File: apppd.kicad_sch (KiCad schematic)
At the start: 99 parts, among them J1 Conn_SWD, J2 APPPD Connector, J4 2601-1102, J5 USB_C_Receptacle_USB2.0_16P, Q1 AO3400A, Q2 AO3400A, Q3 PMV100EPA, SW1 NRST, SW2 BOOT0, U1 AP2112K-3.3, U2 STM32F072CBTx, U3 USBLC6-2SC6, U4 TCAN337, U5 TLV9062xD, U6 LMR33610ADDAR, U7 TLV9062xD, Y1 ABM8AIG-24.000MHz-8-2Z-T

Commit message: update
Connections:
- net GND: now also C29.1
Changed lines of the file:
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@@
 	(text "SMPS"
 		(exclude_from_sim no)
-		(at 244.602 143.002 0)
+		(at 242.824 142.24 0)
 		(effects
 			(font
@@
 	)
 	(symbol
+		(lib_id "Device:C")
+		(at 172.72 226.06 180)
+		(unit 1)
+		(body_style 1)
+		(exclude_from_sim no)
+		(in_bom yes)
+		(on_board yes)
+		(in_pos_files yes)
+		(dnp no)
+		(property "Reference" "C29"
+			(at 175.006 224.79 0)
+			(show_name no)
+			(do_not_autoplace no)
+			(effects
+				(font
+					(size 1.27 1.27)
+				)
+				(justify right)
+			)
+		)
+		(property "Value" "100nF"
+			(at 175.006 227.33 0)
+			(show_name no)
+			(do_not_autoplace no)
+			(effects
+				(font
+					(size 1.27 1.27)
+				)
+				(justify right)
+			)
+		)
+		(property "Footprint" "Capacitor_SMD:C_0402_1005Metric_Pad0.74x0.62mm_HandSolder"
+			(at 171.7548 222.25 0)
+			(hide yes)
+			(show_name no)
+			(do_not_autoplace no)
+			(effects
+				(font
+					(size 1.27 1.27)
+				)
+			)
+		)
+		(property "Datasheet" ""
+			(at 172.72 226.06 0)
+			(hide yes)
+			(show_name no)
+			(do_not_autoplace no)
+			(effects
+				(font
+					(size 1.27 1.27)
+				)
+			)
+		)
+		(property "Description" "Unpolarized capacitor"
+			(at 172.72 226.06 0)
+			(hide yes)
+			(show_name no)
+			(do_not_autoplace no)
+			(effects
+				(font
+					(size 1.27 1.27)
+				)
+			)
+		)
+		(pin "2"
+		)
+		(pin "1"
+		)
+		(instances
+			(project "apppd"
+				(path "/a8b9181f-aad2-4ac0-b955-77d7b04bcf42"
+					(reference "C29")
+					(unit 1)
+				)
+			)
+		)
+	)
+	(symbol
 		(lib_id "power:+12V")
 		(at 186.69 151.13 0)
@@
 					(unit 1)
 				)
-			)
-		)
-	)
-	(symbol
-		(lib_id "Device:C")
-		(at 172.72 224.79 180)
-		(unit 1)
-		(body_style 1)
-		(exclude_from_sim no)
-		(in_bom yes)
-		(on_board yes)
-		(in_pos_files yes)
-		(dnp no)
-		(property "Reference" "C29"
-			(at 175.006 223.52 0)
-			(show_name no)
-			(do_not_autoplace no)
-			(effects
-				(font
-					(size 1.27 1.27)
-				)
-				(justify right)
-			)
-		)
-		(property "Value" "100nF"
-			(at 175.006 226.06 0)
-			(show_name no)
-			(do_not_autoplace no)
-			(effects
-				(font
-					(size 1.27 1.27)
-				)
-				(justify right)
-			)
-		)
-		(property "Footprint" "Capacitor_SMD:C_0402_1005Metric_Pad0.74x0.62mm_HandSolder"
-			(at 171.7548 220.98 0)
-			(hide yes)
-			(show_name no)
-			(do_not_autoplace no)
-			(effects
-				(font
-					(size 1.27 1.27)
-				)
-			)
-		)
-		(property "Datasheet" ""
-			(at 172.72 224.79 0)
-			(hide yes)
-			(show_name no)
-			(do_not_autoplace no)
-			(effects
-				(font
-					(size 1.27 1.27)
-				)
-			)
-		)
-		(property "Description" "Unpolarized capacitor"
-			(at 172.72 224.79 0)
-			(hide yes)
-			(show_name no)
-			(do_not_autoplace no)
-			(effects
-				(font
-					(size 1.27 1.27)
-				)
-			)
-		)
-		(pin "2"
-		)
-		(pin "1"
-		)
-		(instances
-			(project "apppd"
-				(path "/a8b9181f-aad2-4ac0-b955-77d7b04bcf42"
-					(reference "C29")
-					(unit 1)
-				)

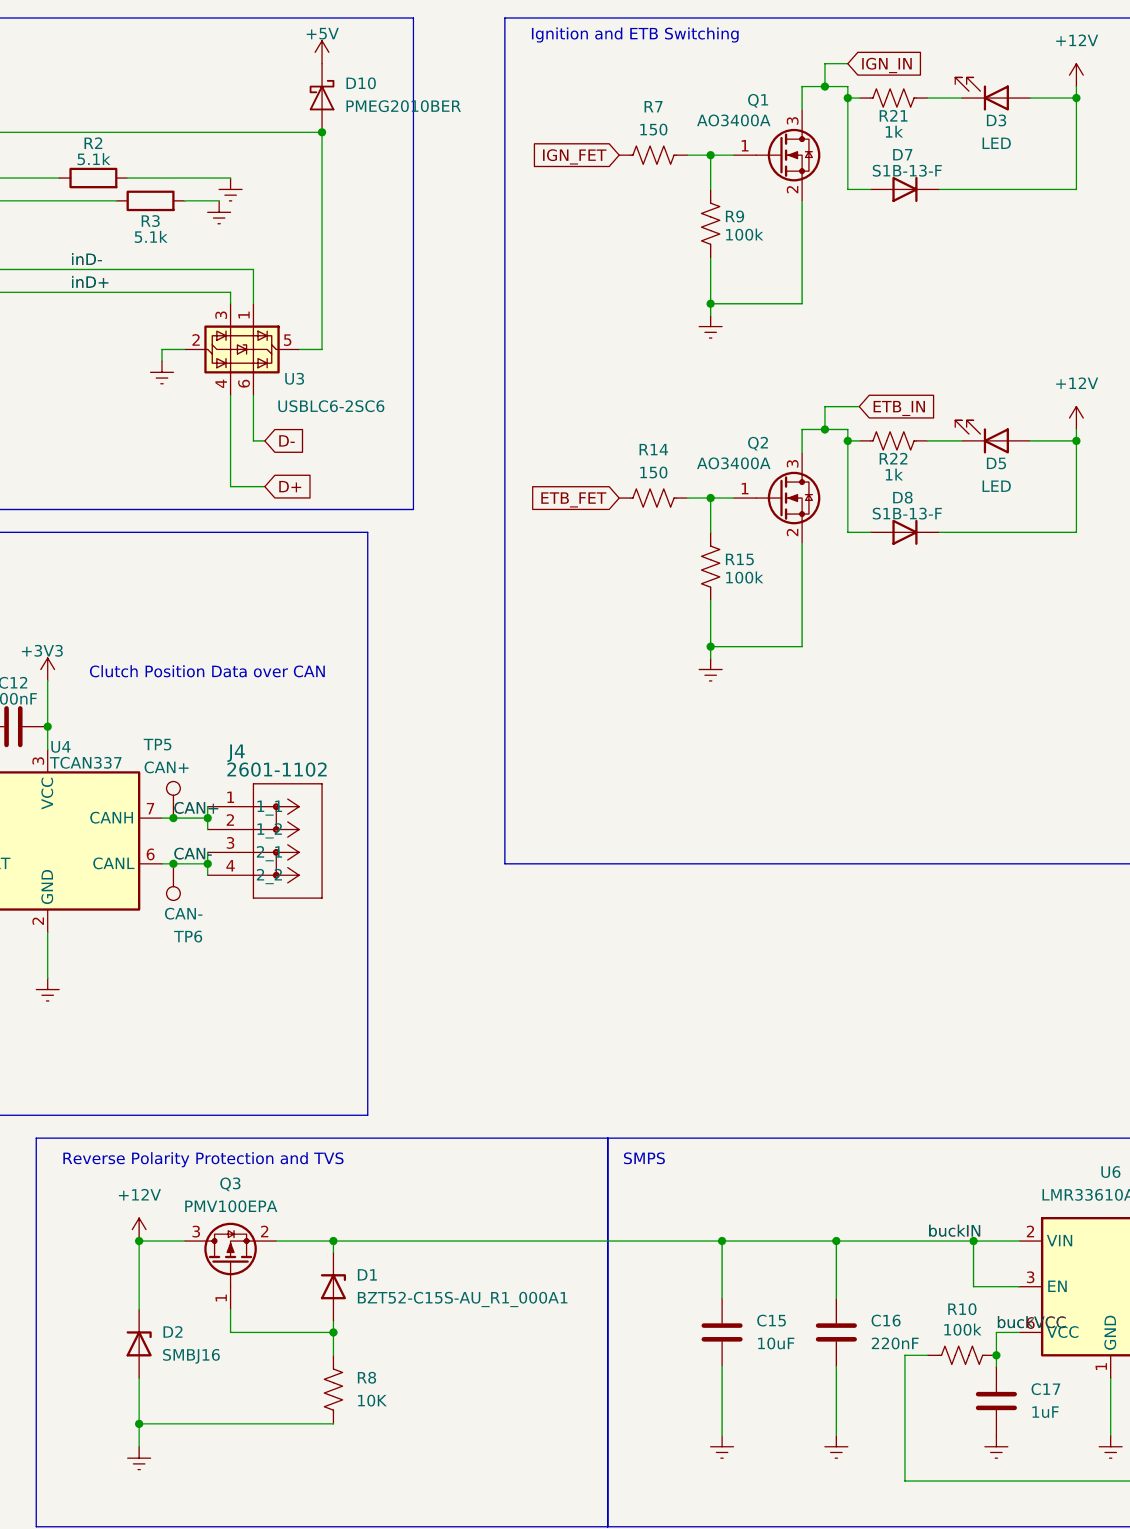
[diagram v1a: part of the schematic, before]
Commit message: Layout progress, still need to do buck
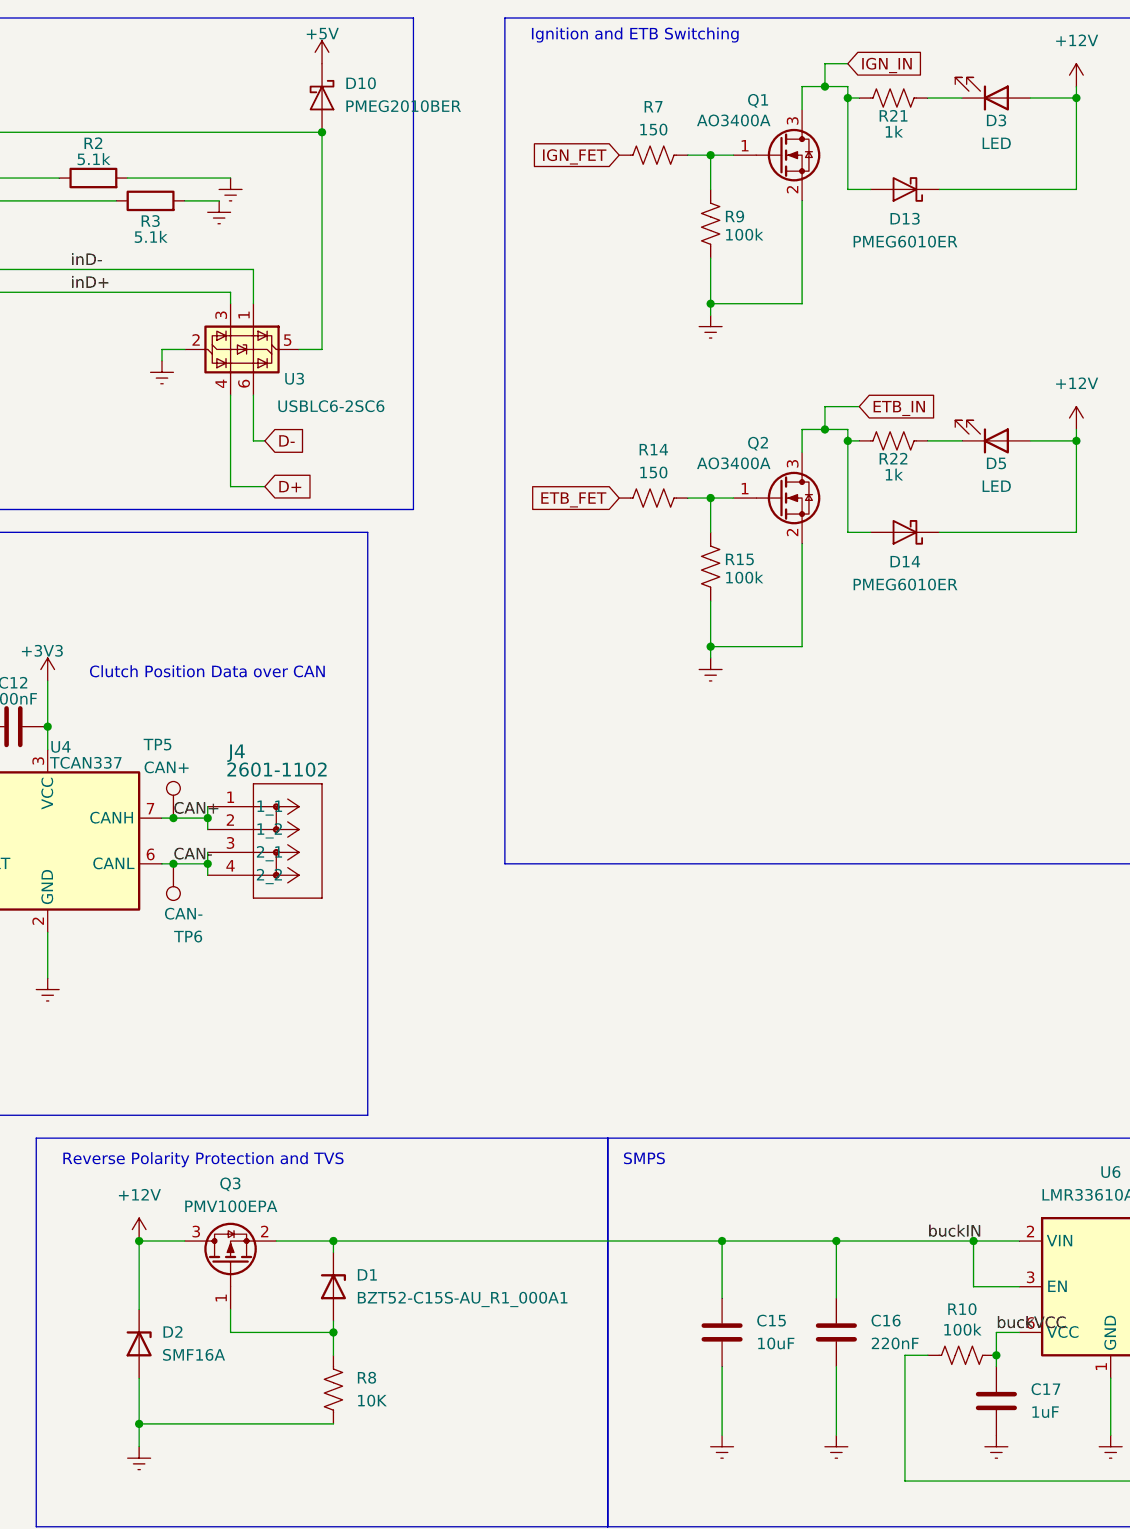
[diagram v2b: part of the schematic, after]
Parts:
- removed D7, D8: S1B-13-F, apppd:S1B-13-F, symbol apppd:S1B-13-F
- added D13, D14: PMEG6010ER, Diode_SMD:Nexperia_CFP3_SOD-123W, symbol Diode:PMEG6010ER
- D2: value SMBJ16 -> SMF16A; footprint apppd:SMBJ16 -> apppd:SMF16A; symbol apppd:SMBJ16 -> apppd:SMF16A; LCSC Part C151254 -> C207257; MPN SMBJ16A -> SMF16A
- Q3: footprint Package_TO_SOT_SMD:TSOT-23_HandSoldering -> Package_TO_SOT_SMD:SOT-23
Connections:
- net +12V: now also D13.1 (K), D14.1 (K)
- net ETB_IN: now also D14.2 (A)
- net IGN_IN: now also D13.2 (A)
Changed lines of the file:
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@@
 	)
 	(symbol
+		(lib_id "Diode:PMEG6010ER")
+		(at 271.78 72.39 180)
+		(unit 1)
+		(body_style 1)
+		(exclude_from_sim no)
+		(in_bom yes)
+		(on_board yes)
+		(in_pos_files yes)
+		(dnp no)
+		(property "Reference" "D14"
+			(at 271.78 75.692 0)
+			(show_name no)
+			(do_not_autoplace no)
+			(effects
+				(font
+					(size 1.27 1.27)
+				)
+			)
+		)
+		(property "Value" "PMEG6010ER"
+			(at 271.78 78.232 0)
+			(show_name no)
+			(do_not_autoplace no)
+			(effects
+				(font
+					(size 1.27 1.27)
+				)
+			)
+		)
+		(property "Footprint" "Diode_SMD:Nexperia_CFP3_SOD-123W"
+			(at 271.78 67.945 0)
+			(hide yes)
+			(show_name no)
+			(do_not_autoplace no)
+			(effects
+				(font
+					(size 1.27 1.27)
+				)
+			)
+		)
+		(property "Datasheet" "https://assets.nexperia.com/documents/data-sheet/PMEG6010ER.pdf"
+			(at 271.78 72.39 0)
+			(hide yes)
+			(show_name no)
+			(do_not_autoplace no)
+			(effects
+				(font
+					(size 1.27 1.27)
+				)
+			)
+		)
+		(property "Description" "60V, 1A low Vf MEGA Schottky barrier rectifier, SOD-123W"
+			(at 271.78 72.39 0)
+			(hide yes)
+			(show_name no)
+			(do_not_autoplace no)
+			(effects
+				(font
+					(size 1.27 1.27)
+				)
+			)
+		)
+		(pin "1"
+		)
+		(pin "2"
+		)
+		(instances
+			(project "apppd"
+				(path "/a8b9181f-aad2-4ac0-b955-77d7b04bcf42"
+					(reference "D14")
+					(unit 1)
+				)
+			)
+		)
+	)
+	(symbol
 		(lib_id "Connector:TestPoint")
 		(at 81.28 29.21 0)
@@
 	)
 	(symbol
-		(lib_id "apppd:S1B-13-F")
-		(at 271.78 72.39 180)
-		(unit 1)
-		(body_style 1)
-		(exclude_from_sim no)
-		(in_bom yes)
-		(on_board yes)
-		(in_pos_files yes)
-		(dnp no)
-		(property "Reference" "D8"
-			(at 271.526 68.58 0)
-			(show_name no)
-			(do_not_autoplace no)
-			(effects
-				(font
-					(size 1.27 1.27)
-				)
-			)
-		)
-		(property "Value" "S1B-13-F"
-			(at 272.034 70.358 0)
-			(show_name no)
-			(do_not_autoplace no)
-			(effects
-				(font
-					(size 1.27 1.27)
-				)
-			)
-		)
-		(property "Footprint" "apppd:S1B-13-F"
-			(at 271.78 72.39 0)
-			(hide yes)
-			(show_name no)
-			(do_not_autoplace no)
-			(effects
-				(font
-					(size 1.27 1.27)
-				)
-			)
-		)
-		(property "Datasheet" "https://www.diodes.com/part/view/S1B"
-			(at 271.78 72.39 0)
-			(hide yes)
-			(show_name no)
-			(do_not_autoplace no)
-			(effects
-				(font
-					(size 1.27 1.27)
-				)
-			)
-		)
-		(property "Description" "100V 1A general purpose glass passivated rectifier, Vf 1.1V max @ 1A, IFSM 30A, DO-214AC (SMA)"
-			(at 271.78 72.39 0)
-			(hide yes)
-			(show_name no)
-			(do_not_autoplace no)
-			(effects
-				(font
-					(size 1.27 1.27)
-				)
-			)
-		)
-		(property "Manufacturer" "Diodes Incorporated"
-			(at 271.78 72.39 0)
-			(hide yes)
-			(show_name no)
-			(do_not_autoplace no)
-			(effects
-				(font
-					(size 1.27 1.27)
-				)
-			)
-		)
-		(property "MPN" "S1B-13-F"
-			(at 271.78 72.39 0)
-			(hide yes)
-			(show_name no)
-			(do_not_autoplace no)
-			(effects
-				(font
-					(size 1.27 1.27)
-				)
-			)
-		)
-		(property "LCSC Part" "C156295"
-			(at 271.78 72.39 0)
-			(hide yes)
-			(show_name no)
-			(do_not_autoplace no)
-			(effects
-				(font
-					(size 1.27 1.27)
-				)
-			)
-		)
-		(pin "1"
-		)
-		(pin "2"
-		)
-		(instances
-			(project "apppd"
-				(path "/a8b9181f-aad2-4ac0-b955-77d7b04bcf42"
-					(reference "D8")
-					(unit 1)
-				)
-			)
-		)
-	)
-	(symbol
 		(lib_id "Device:C")
 		(at 102.87 60.96 0)
@@
 	)
 	(symbol
-		(lib_id "apppd:S1B-13-F")
-		(at 271.78 34.29 180)
-		(unit 1)
-		(body_style 1)
-		(exclude_from_sim no)
-		(in_bom yes)
-		(on_board yes)
-		(in_pos_files yes)
-		(dnp no)
-		(property "Reference" "D7"
-			(at 271.526 30.48 0)
-			(show_name no)
-			(do_not_autoplace no)
-			(effects
-				(font
-					(size 1.27 1.27)
-				)
-			)
-		)
-		(property "Value" "S1B-13-F"
-			(at 272.034 32.258 0)
-			(show_name no)
-			(do_not_autoplace no)
-			(effects
-				(font
-					(size 1.27 1.27)
-				)
-			)
-		)
-		(property "Footprint" "apppd:S1B-13-F"
-			(at 271.78 34.29 0)
-			(hide yes)
-			(show_name no)
-			(do_not_autoplace no)
-			(effects
-				(font
-					(size 1.27 1.27)
-				)
-			)
-		)
-		(property "Datasheet" "https://www.diodes.com/part/view/S1B"
-			(at 271.78 34.29 0)
-			(hide yes)
-			(show_name no)
-			(do_not_autoplace no)
-			(effects
-				(font
-					(size 1.27 1.27)
-				)
-			)
-		)
-		(property "Description" "100V 1A general purpose glass passivated rectifier, Vf 1.1V max @ 1A, IFSM 30A, DO-214AC (SMA)"
-			(at 271.78 34.29 0)
-			(hide yes)
-			(show_name no)
-			(do_not_autoplace no)
-			(effects
-				(font
-					(size 1.27 1.27)
-				)
-			)
-		)
-		(property "Manufacturer" "Diodes Incorporated"
-			(at 271.78 34.29 0)
-			(hide yes)
-			(show_name no)
-			(do_not_autoplace no)
-			(effects
-				(font
-					(size 1.27 1.27)
-				)
-			)
-		)
-		(property "MPN" "S1B-13-F"
-			(at 271.78 34.29 0)
-			(hide yes)
-			(show_name no)
-			(do_not_autoplace no)
-			(effects
-				(font
-					(size 1.27 1.27)
-				)
-			)
-		)
-		(property "LCSC Part" "C156295"
-			(at 271.78 34.29 0)
-			(hide yes)
-			(show_name no)
-			(do_not_autoplace no)
-			(effects
-				(font
-					(size 1.27 1.27)
-				)
-			)
-		)
-		(pin "1"
-		)
-		(pin "2"
-		)
-		(instances
-			(project "apppd"
-				(path "/a8b9181f-aad2-4ac0-b955-77d7b04bcf42"
-					(reference "D7")
-					(unit 1)
-				)
-			)
-		)
-	)
-	(symbol
 		(lib_id "EasyEDA:TS-1088-AR02016")
 		(at 36.83 113.03 0)
@@
 	)
 	(symbol
+		(lib_id "Diode:PMEG6010ER")
+		(at 271.78 34.29 180)
+		(unit 1)
+		(body_style 1)
+		(exclude_from_sim no)
+		(in_bom yes)
+		(on_board yes)
+		(in_pos_files yes)
+		(dnp no)
+		(property "Reference" "D13"
+			(at 271.78 37.592 0)
+			(show_name no)
+			(do_not_autoplace no)
+			(effects
+				(font
+					(size 1.27 1.27)
+				)
+			)
+		)
+		(property "Value" "PMEG6010ER"
+			(at 271.78 40.132 0)
+			(show_name no)
+			(do_not_autoplace no)
+			(effects
+				(font
+					(size 1.27 1.27)
+				)
+			)
+		)
+		(property "Footprint" "Diode_SMD:Nexperia_CFP3_SOD-123W"
+			(at 271.78 29.845 0)
+			(hide yes)
+			(show_name no)
+			(do_not_autoplace no)
+			(effects
+				(font
+					(size 1.27 1.27)
+				)
+			)
+		)
+		(property "Datasheet" "https://assets.nexperia.com/documents/data-sheet/PMEG6010ER.pdf"
+			(at 271.78 34.29 0)
+			(hide yes)
+			(show_name no)
+			(do_not_autoplace no)
+			(effects
+				(font
+					(size 1.27 1.27)
+				)
+			)
+		)
+		(property "Description" "60V, 1A low Vf MEGA Schottky barrier rectifier, SOD-123W"
+			(at 271.78 34.29 0)
+			(hide yes)
+			(show_name no)
+			(do_not_autoplace no)
+			(effects
+				(font
+					(size 1.27 1.27)
+				)
+			)
+		)
+		(pin "1"
+		)
+		(pin "2"
+		)
+		(instances
+			(project "apppd"
+				(path "/a8b9181f-aad2-4ac0-b955-77d7b04bcf42"
+					(reference "D13")
+					(unit 1)
+				)
+			)
+		)
+	)
+	(symbol
 		(lib_id "power:Earth")
 		(at 102.87 87.63 0)
@@
 	)
 	(symbol
-		(lib_id "apppd:SMBJ16")
+		(lib_id "apppd:SMF16A")
 		(at 186.69 162.56 270)
 		(unit 1)
@@
 			)
 		)
-		(property "Value" "SMBJ16"
+		(property "Value" "SMF16A"
 			(at 189.23 163.8299 90)
 			(show_name no)
@@
 			)
 		)
-		(property "Footprint" "apppd:SMBJ16"
+		(property "Footprint" "apppd:SMF16A"
 			(at 186.69 162.56 0)
 			(hide yes)
@@
 			)
 		)
-		(property "Datasheet" "https://www.littelfuse.com/assetdocs/tvs-diodes-smbj-series-datasheet?assetguid=ba555e99-a12d-4f72-a0b6-86b06c67171e"
+		(property "Datasheet" "https://www.littelfuse.com/products/overvoltage-protection/tvs-diodes/surface-mount/smf/smf16a"
 			(at 186.69 162.56 0)
 			(hide yes)
@@
 			)
 		)
-		(property "Description" "600W unidirectional TVS diode, Vrwm 16V, Vbr 17.8-19.7V, Vc 26V max @ Ipp 23.1A (10/1000us), DO-214AA (SMB)"
+		(property "Description" "200W unidirectional TVS diode, Vrwm 16V, Vbr 17.8-19.7V, Vc 26V max @ Ipp 7.2A (10/1000us), SOD-123FL"
 			(at 186.69 162.56 0)
 			(hide yes)
@@
 			)
 		)
-		(property "MPN" "SMBJ16A"
+		(property "MPN" "SMF16A"
 			(at 186.69 162.56 0)
 			(hide yes)
@@
 			)
 		)
-		(property "LCSC Part" "C151254"
+		(property "LCSC Part" "C207257"
 			(at 186.69 162.56 0)
 			(hide yes)
@@
 			)
 		)
-		(property "Footprint" "Package_TO_SOT_SMD:TSOT-23_HandSoldering"
+		(property "Footprint" "Package_TO_SOT_SMD:SOT-23"
 			(at 198.755 148.59 0)
 			(hide yes)
